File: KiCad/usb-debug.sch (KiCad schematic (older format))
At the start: 76 parts, among them IC1 TPS7A0518PDBVT, IC16 AP22652W6-7, IC7 HD3SS3220, J11 632723300011, J5 632723300011, J9 632723300011, Q1 PMV32UP, T6 BSS138APW, T7 BSS138APW, U10 TPD4E05U06QDQARQ1, U11 TPD4E05U06QDQARQ1, U12 TPD4E05U06QDQARQ1, U13 TPD4E05U06QDQARQ1, U8 TPD4E05U06QDQARQ1, U9 TPD4E05U06QDQARQ1

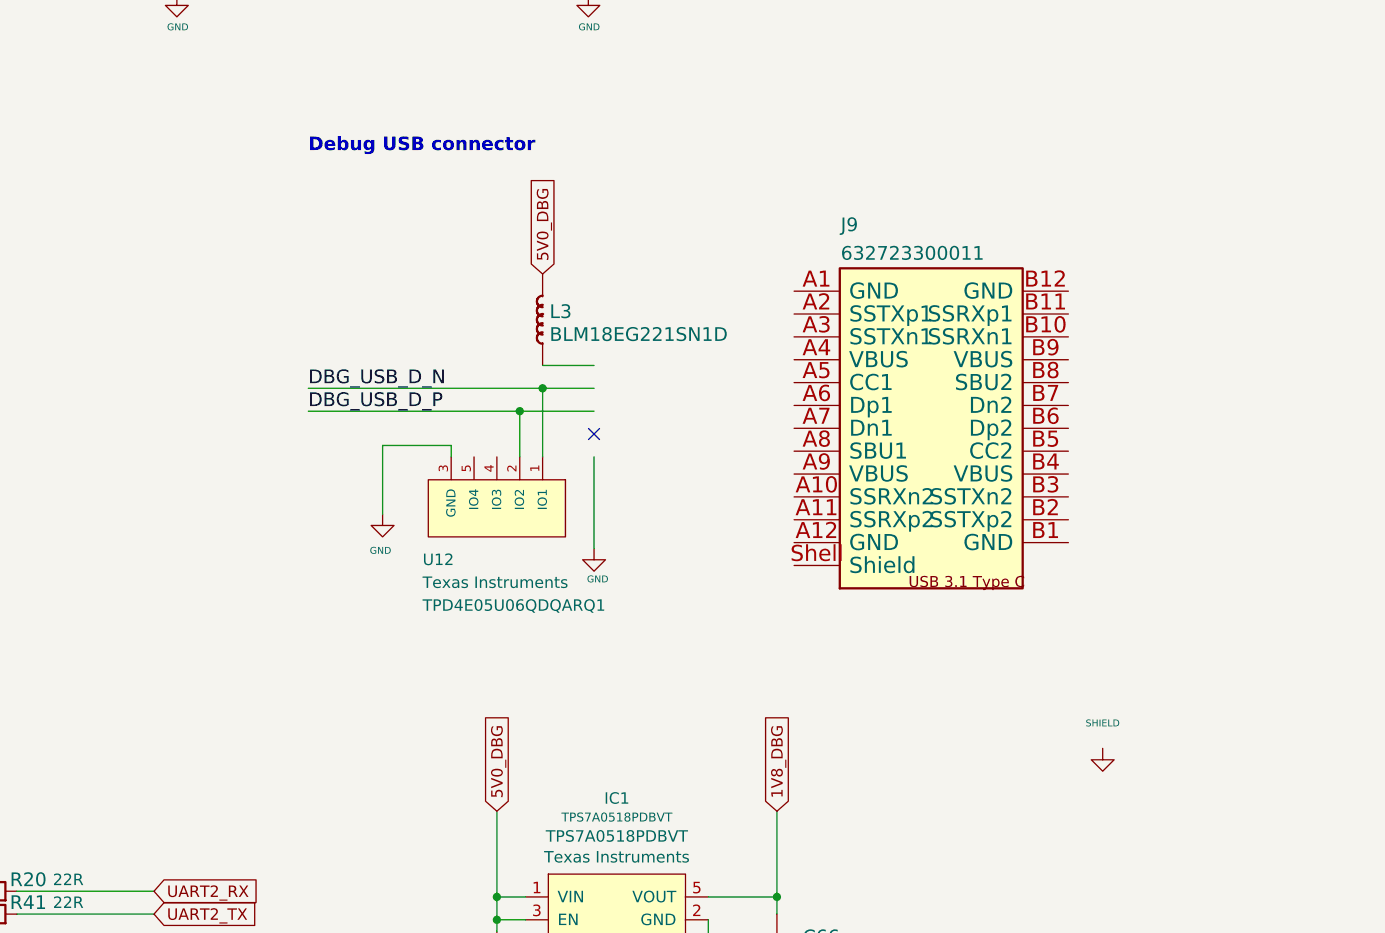
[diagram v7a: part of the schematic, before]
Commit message: Wire signals to debug USB-C connector
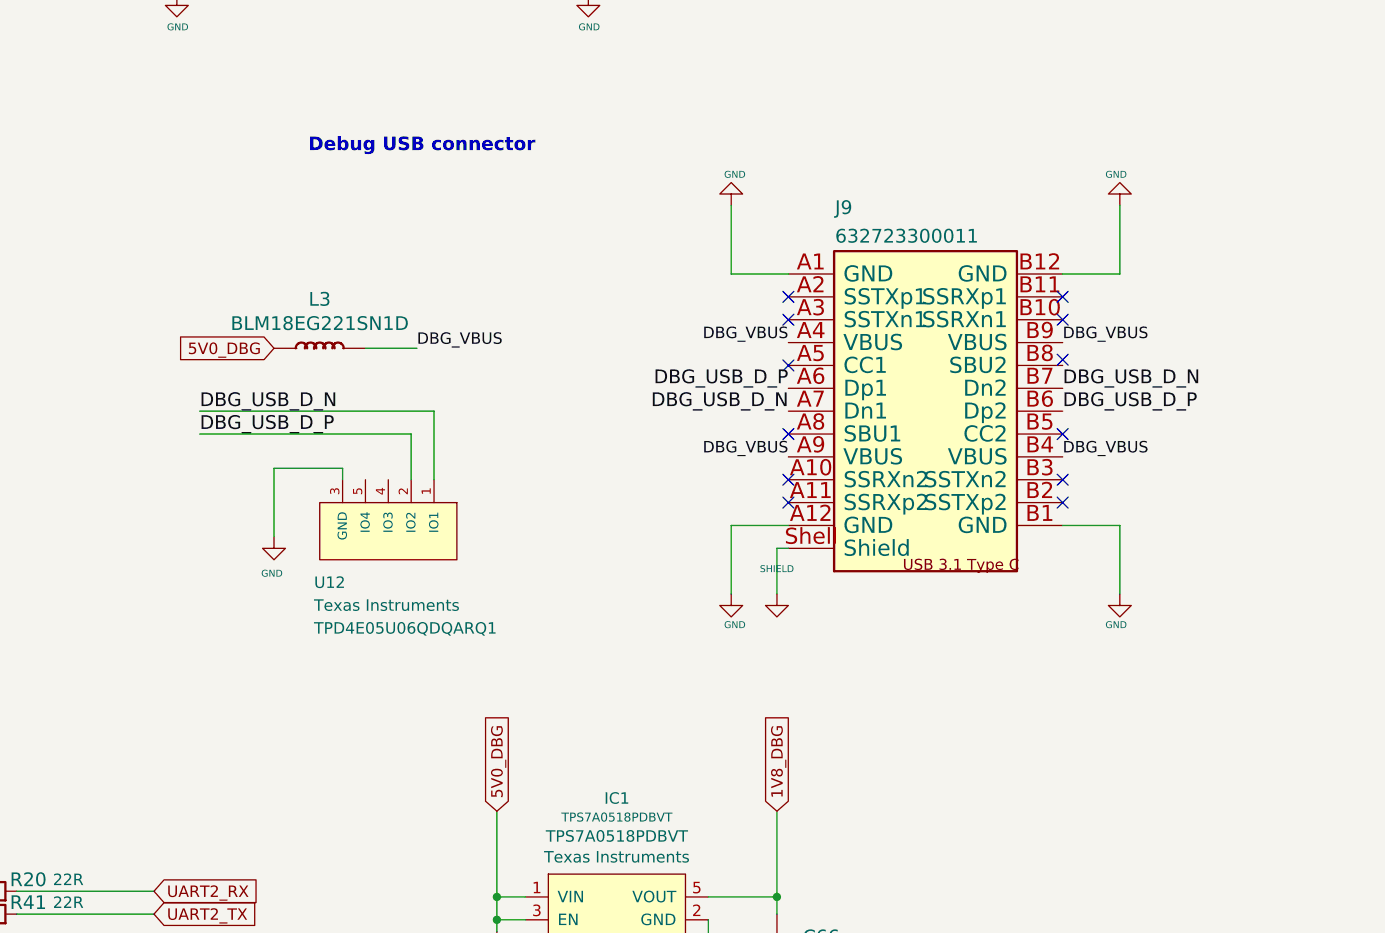
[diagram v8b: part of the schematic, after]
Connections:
- net labels added: DBG_VBUS
- wire segments 258 -> 265
- no-connect marks 18 -> 29
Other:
- moved on the sheet: J9, L3, U12
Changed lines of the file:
@@
 Text Notes 2669 49363 0    60   ~ 0
 Text
-Text Label 12350 6825 0    60   ~ 0
+Text Label 11875 6925 0    60   ~ 0
 DBG_USB_D_N
-Text Label 12350 6925 0    60   ~ 0
+Text Label 11875 7025 0    60   ~ 0
 DBG_USB_D_P
 Text Notes 12350 5800 0    59   ~ 12
@@
 Text GLabel 14400 8675 1    50   Input ~ 0
 1V8_DBG
-Text GLabel 13375 6325 1    50   Input ~ 0
+Text GLabel 12200 6650 0    50   Input ~ 0
 5V0_DBG
 Text GLabel 11325 2125 1    50   Input ~ 0
@@
 L jetson-nano-baseboard:GND #GND_086
 U 1 1 5E71036D
-P 13600 7525
-F 0 "#GND_086" H 13600 7525 20  0001 C CNN
-F 1 "GND" H 13616 7390 30  0000 C CNN
-F 2 "" H 13600 7525 70  0001 C CNN
-F 3 "" H 13600 7525 70  0001 C CNN
-	1    13600 7525
+P 14200 7725
+F 0 "#GND_086" H 14200 7725 20  0001 C CNN
+F 1 "GND" H 14216 7590 30  0000 C CNN
+F 2 "" H 14200 7725 70  0001 C CNN
+F 3 "" H 14200 7725 70  0001 C CNN
+	1    14200 7725
 	1    0    0    -1
 $EndComp
@@
 L jetson-nano-baseboard:GND #GND_087
 U 1 1 5E71036C
-P 12675 7375
-F 0 "#GND_087" H 12675 7375 20  0001 C CNN
-F 1 "GND" H 12666 7215 30  0000 C CNN
-F 2 "" H 12675 7375 70  0001 C CNN
-F 3 "" H 12675 7375 70  0001 C CNN
-	1    12675 7375
+P 12200 7475
+F 0 "#GND_087" H 12200 7475 20  0001 C CNN
+F 1 "GND" H 12191 7315 30  0000 C CNN
+F 2 "" H 12200 7475 70  0001 C CNN
+F 3 "" H 12200 7475 70  0001 C CNN
+	1    12200 7475
 	1    0    0    -1
 $EndComp
@@
 L jetson-nano-baseboard:GND #SHIELD01
 U 1 1 5E71036B
-P 15825 8400
-F 0 "#SHIELD01" H 15825 8540 20  0001 C CNN
-F 1 "SHIELD" H 15825 8510 30  0000 C CNN
-F 2 "" H 15825 8400 70  0001 C CNN
-F 3 "" H 15825 8400 70  0001 C CNN
-	1    15825 8400
+P 14400 7725
+F 0 "#SHIELD01" H 14400 7865 20  0001 C CNN
+F 1 "SHIELD" H 14400 7835 30  0000 C CNN
+F 2 "" H 14400 7725 70  0001 C CNN
+F 3 "" H 14400 7725 70  0001 C CNN
+	1    14400 7725
 	1    0    0    -1
 $EndComp
@@
 	5375 8975 5775 8975
 Wire Wire Line
-	13600 7125 13600 7525
-Wire Wire Line
-	13600 6925 13275 6925
-Wire Wire Line
-	12675 7075 12675 7375
-Wire Wire Line
-	13275 7125 13275 6925
-Connection ~ 13275 6925
-Wire Wire Line
-	13275 6925 12350 6925
-Wire Wire Line
-	13375 7125 13375 6825
-Wire Wire Line
-	12350 6825 13375 6825
-Connection ~ 13375 6825
-Wire Wire Line
-	13375 6825 13600 6825
-Wire Wire Line
-	13600 6725 13375 6725
-NoConn ~ 13600 7025
+	12200 7175 12200 7475
+Wire Wire Line
+	12800 7225 12800 7025
+Wire Wire Line
+	12800 7025 11875 7025
+Wire Wire Line
+	12900 7225 12900 6925
+Wire Wire Line
+	11875 6925 12900 6925
+Wire Wire Line
+	12825 6650 12600 6650
 Wire Wire Line
 	9000 9125 8500 9125
@@
 	11775 4875 11775 5100
 Wire Wire Line
-	12975 7075 12675 7075
+	12500 7175 12200 7175
 $Comp
 L antmicroTVSDiodes:TPD4E05U06QDQARQ1 U12
 U 1 1 62017093
-P 13175 7175
-F 0 "U12" V 13575 6850 50  0000 L CNN
-F 1 "TPD4E05U06QDQARQ1" H 13225 6775 50  0001 L CNN
-F 2 "antmicro-footprints:TPD4E05U06QDQARQ1" H 13225 7625 50  0001 L CNN
-F 3 "http://www.ti.com/general/docs/lit/getliterature.tsp?genericPartNumber=TPD4E001&fileType=pdf" H 13175 7575 50  0001 L CNN
-F 4 "Texas Instruments" V 13675 6850 50  0000 L CNN "Manufacturer"
-F 5 "TPD4E05U06QDQARQ1" V 13775 6850 50  0000 L CNN "MPN"
-	1    13175 7175
+P 12700 7275
+F 0 "U12" V 13100 6950 50  0000 L CNN
+F 1 "TPD4E05U06QDQARQ1" H 12750 6875 50  0001 L CNN
+F 2 "antmicro-footprints:TPD4E05U06QDQARQ1" H 12750 7725 50  0001 L CNN
+F 3 "http://www.ti.com/general/docs/lit/getliterature.tsp?genericPartNumber=TPD4E001&fileType=pdf" H 12700 7675 50  0001 L CNN
+F 4 "Texas Instruments" V 13200 6950 50  0000 L CNN "Manufacturer"
+F 5 "TPD4E05U06QDQARQ1" V 13300 6950 50  0000 L CNN "MPN"
+	1    12700 7275
 	0    1    1    0
 $EndComp
 Wire Wire Line
-	12975 7075 12975 7125
+	12500 7175 12500 7225
 Wire Wire Line
 	7625 6550 7625 6600
@@
 L jetson-nano-baseboard:BLM18EG221SN1D L3
 U 1 1 5E7102ED
-P 13375 6525
-F 0 "L3" V 13375 6495 60  0000 R TNN
-F 1 "BLM18EG221SN1D" V 13275 6495 60  0000 R TNN
-F 2 "jetson-nano-baseboard-footprints:0603" H 13275 6495 60  0001 C CNN
-F 3 "" H 13275 6495 60  0001 C CNN
-F 4 "BLM18EG221SN1D" H -24985 -20787 50  0001 C CNN "MPN"
-F 5 "Murata" H -24985 -20787 50  0001 C CNN "Manufacturer"
-	1    13375 6525
-	0    -1   -1   0
+P 12400 6650
+F 0 "L3" H 12400 6864 60  0000 C CNN
+F 1 "BLM18EG221SN1D" H 12400 6758 60  0000 C CNN
+F 2 "jetson-nano-baseboard-footprints:0603" H 12300 6620 60  0001 C CNN
+F 3 "" H 12300 6620 60  0001 C CNN
+F 4 "BLM18EG221SN1D" H -25960 -20662 50  0001 C CNN "MPN"
+F 5 "Murata" H -25960 -20662 50  0001 C CNN "Manufacturer"
+	1    12400 6650
+	-1   0    0    -1
 $EndComp
 $Comp
@@
 L jetson-nano-baseboard:WE_632723300011 J9
 U 1 1 6285123F
-P 14675 6300
-F 0 "J9" H 14679 6455 60  0000 L BNN
-F 1 "632723300011" H 14679 6330 60  0000 L BNN
-F 2 "jetson-nano-baseboard-footprints:WE_632723300011" H 14675 6300 60  0001 C CNN
-F 3 "" H 14675 6300 60  0001 C CNN
-F 4 "Wurth Elektronik" V 3975 1707 60  0001 C CNN "Manufacturer"
-F 5 "632723300011" H -28296 -9805 50  0001 C CNN "MPN"
-	1    14675 6300
-	1    0    0    -1
-$EndComp
+P 14650 6225
+F 0 "J9" H 14654 6380 60  0000 L BNN
+F 1 "632723300011" H 14654 6255 60  0000 L BNN
+F 2 "jetson-nano-baseboard-footprints:WE_632723300011" H 14650 6225 60  0001 C CNN
+F 3 "" H 14650 6225 60  0001 C CNN
+F 4 "Wurth Elektronik" V 3950 1632 60  0001 C CNN "Manufacturer"
+F 5 "632723300011" H -28321 -9880 50  0001 C CNN "MPN"
+	1    14650 6225
+	1    0    0    -1
+$EndComp
+Text Label 14450 7125 2    50   ~ 0
+DBG_VBUS
+Text Label 14450 6625 2    50   ~ 0
+DBG_VBUS
+Text Label 12825 6650 0    50   ~ 0
+DBG_VBUS
+Wire Wire Line
+	14450 7525 14400 7525
+Wire Wire Line
+	14400 7525 14400 7725
+Wire Wire Line
+	14450 7425 14200 7425
+Wire Wire Line
+	14200 7425 14200 7725
+Text Label 14450 6925 2    60   ~ 0
+DBG_USB_D_N
+Text Label 14450 6825 2    60   ~ 0
+DBG_USB_D_P
+$Comp
+L jetson-nano-baseboard:GND #GND_0123
+U 1 1 61E4DC90
+P 15900 7725
+F 0 "#GND_0123" H 15900 7725 20  0001 C CNN
+F 1 "GND" H 15916 7590 30  0000 C CNN
+F 2 "" H 15900 7725 70  0001 C CNN
+F 3 "" H 15900 7725 70  0001 C CNN
+	1    15900 7725
+	-1   0    0    -1
+$EndComp
+Wire Wire Line
+	15650 7425 15900 7425
+Wire Wire Line
+	15900 7425 15900 7725
+$Comp
+L jetson-nano-baseboard:GND #GND_0124
+U 1 1 61E61C5D
+P 15900 6025
+F 0 "#GND_0124" H 15900 6025 20  0001 C CNN
+F 1 "GND" H 15916 5890 30  0000 C CNN
+F 2 "" H 15900 6025 70  0001 C CNN
+F 3 "" H 15900 6025 70  0001 C CNN
+	1    15900 6025
+	-1   0    0    1
+$EndComp
+Wire Wire Line
+	15650 6325 15900 6325
+Wire Wire Line
+	15900 6325 15900 6025
+$Comp
+L jetson-nano-baseboard:GND #GND_0125
+U 1 1 61E75831
+P 14200 6025
+F 0 "#GND_0125" H 14200 6025 20  0001 C CNN
+F 1 "GND" H 14216 5890 30  0000 C CNN
+F 2 "" H 14200 6025 70  0001 C CNN
+F 3 "" H 14200 6025 70  0001 C CNN
+	1    14200 6025
+	1    0    0    1
+$EndComp
+Wire Wire Line
+	14450 6325 14200 6325
+Wire Wire Line
+	14200 6325 14200 6025
+Text Label 15650 6825 0    60   ~ 0
+DBG_USB_D_N
+Text Label 15650 6925 0    60   ~ 0
+DBG_USB_D_P
+Text Label 15650 6625 0    50   ~ 0
+DBG_VBUS
+Text Label 15650 7125 0    50   ~ 0
+DBG_VBUS
+NoConn ~ 14450 6425
+NoConn ~ 14450 6525
+NoConn ~ 14450 6725
+NoConn ~ 14450 7025
+NoConn ~ 14450 7225
+NoConn ~ 14450 7325
+NoConn ~ 15650 7225
+NoConn ~ 15650 7325
+NoConn ~ 15650 7025
+NoConn ~ 15650 6700
+NoConn ~ 15650 6525
+NoConn ~ 15650 6425
 $EndSCHEMATC
